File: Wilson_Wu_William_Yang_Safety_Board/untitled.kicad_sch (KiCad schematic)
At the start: 32 parts, among them J18 XT60-M, J3 430450200, J5 430450200, J6 XT60-M, J7 XT60-M, Q1 IRLML6344TRPBF, Q2 IRLML6344TRPBF, U12 J115F11AH12VDCS61.5U, U13 ISOM8110DFGRQ1, U16 J115F11AH12VDCS61.5U, U5 J115F11AH12VDCS61.5U, U6 J115F11AH12VDCS61.5U

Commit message: layout
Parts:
- removed TP12: TestPoint, TestPoint:TestPoint_Pad_D1.0mm, symbol Connector:TestPoint
- added load_neg_tp1, mosfet_drain_tp1, mosfet_drain_tp2, source_pos_tp1, source_pos_tp2: V_DIVIDED, TestPoint:TestPoint_Pad_D1.0mm, symbol Connector:TestPoint
- renumbered TP8 to ESTOP_TP1, TP_48V6 to HFC_NEG_TP1, TP_48V5 to HFC_RELAY_TP1, TP4 to RELAY_O_TP1, TP13 to load_pos_tp1
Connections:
- net DRAIN: now also mosfet_drain_tp1.1
- net load negative: now also load_neg_tp1.1
- net source negative: now also source_pos_tp1.1
- net source_conn: now also source_pos_tp2.1
- net at D2.2 (A), Q2.3, U5.2 (COIL_2): now also mosfet_drain_tp2.1

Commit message: update
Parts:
- added R_6: 0, Resistor_SMD:R_0805_2012Metric, symbol Device:R_US
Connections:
- net DRAIN: no longer names the net of D1.2 (A), Q1.3, U6.1 (COIL_1), mosfet_drain_tp1.1
- net DRAIN: now also R_6.2; no longer D7.2 (A), U12.2 (COIL_2)
- new net drain: D7.2 (A), R_6.1, U12.2 (COIL_2)
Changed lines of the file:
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@@
+	)
+	(junction
+		(at 142.24 50.8)
+		(diameter 0)
+		(color 0 0 0 0)
 	)
 	(junction
@@
 		(pts
 			(xy 142.24 31.75) (xy 142.24 46.99)
+		)
+		(stroke
+			(width 0)
+			(type default)
+		)
+	)
+	(wire
+		(pts
+			(xy 142.24 50.8) (xy 151.13 50.8)
 		)
 		(stroke
@@
 		)
 	)
-	(label "DRAIN"
-		(at 142.24 50.8 0)
-		(effects
-			(font
-				(size 1.27 1.27)
-			)
-			(justify left bottom)
-		)
-	)
-	(label "DRAIN"
-		(at 160.02 111.76 90)
-		(effects
-			(font
-				(size 1.27 1.27)
-			)
-			(justify left bottom)
-		)
-	)
 	(label "source negative"
 		(at 40.64 36.83 270)
@@
 			)
 			(justify left bottom)
+		)
+	)
+	(global_label "drain"
+		(shape input)
+		(at 158.75 50.8 0)
+		(fields_autoplaced yes)
+		(effects
+			(font
+				(size 1.27 1.27)
+			)
+			(justify left)
+		)
+		(property "Intersheetrefs" "${INTERSHEET_REFS}"
+			(at 166.5732 50.8 0)
+			(effects
+				(font
+					(size 1.27 1.27)
+				)
+				(justify left)
+				(hide yes)
+			)
 		)
 	)
@@
 				)
 				(justify right)
+				(hide yes)
+			)
+		)
+	)
+	(global_label "drain"
+		(shape input)
+		(at 160.02 111.76 90)
+		(fields_autoplaced yes)
+		(effects
+			(font
+				(size 1.27 1.27)
+			)
+			(justify left)
+		)
+		(property "Intersheetrefs" "${INTERSHEET_REFS}"
+			(at 160.02 103.9368 90)
+			(effects
+				(font
+					(size 1.27 1.27)
+				)
+				(justify left)
 				(hide yes)
 			)
@@
 					(unit 1)
 				)
+			)
+		)
+	)
+	(symbol
+		(lib_id "Device:R_US")
+		(at 154.94 50.8 270)
+		(unit 1)
+		(exclude_from_sim no)
+		(in_bom yes)
+		(on_board yes)
+		(dnp no)
+		(property "Reference" "R_6"
+			(at 154.94 54.864 90)
+			(effects
+				(font
+					(size 1.27 1.27)
+				)
+			)
+		)
+		(property "Value" "0"
+			(at 154.94 52.832 90)
+			(effects
+				(font
+					(size 1.27 1.27)
+				)
+			)
+		)
+		(property "Footprint" "Resistor_SMD:R_0805_2012Metric"
+			(at 154.686 51.816 90)
+			(effects
+				(font
+					(size 1.27 1.27)
+				)
+				(hide yes)
+			)
+		)
+		(property "Datasheet" "~"
+			(at 154.94 50.8 0)
+			(effects
+				(font
+					(size 1.27 1.27)
+				)
+				(hide yes)
+			)
+		)
+		(property "Description" "Resistor, US symbol"
+			(at 154.94 50.8 0)
+			(effects
+				(font
+					(size 1.27 1.27)
+				)
+				(hide yes)
+			)
+		)
+		(pin "1"
+		)
+		(pin "2"
+		)
+		(instances
+			(project "Wilson_Wu_William_Yang_Safety_Board"
+				(path "/fa857c32-0741-4b91-b122-1a57686bb514/3aab1625-1497-4612-8772-a9d051eba0fa"
+					(reference "R_6")
+					(unit 1)
+				)

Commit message: update
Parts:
- added D9: LED, LED_SMD:LED_Foshan-NTD3528_3.5x2.8mm, symbol Device:LED
- added R21: 10k, Resistor_SMD:R_0805_2012Metric, symbol Device:R_US
- R7: value 10k -> 0
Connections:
- net source negative is gone; now on net GND: J6.N (NEG), U5.4 (COM), source_pos_tp1.1
- net +12V: no longer R2.2
- net GND: now also D9.1 (K)
- net drain: now also R2.2
- net at D2.2 (A), Q2.3, U5.2 (COIL_2)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: now also R21.2
- new net: D9.2 (A), R21.1
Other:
- moved on the sheet: D6, R2, source_pos_tp1

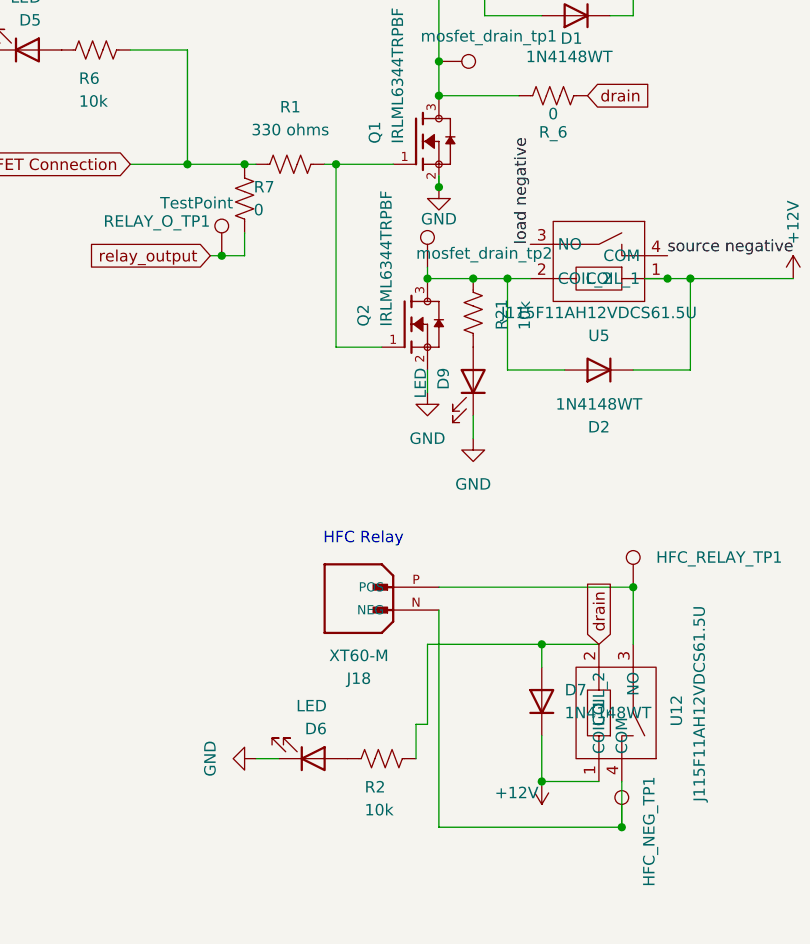
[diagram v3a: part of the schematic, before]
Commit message: LED Changes
-Fixed LED so that Relay U5 wouldn't always be on
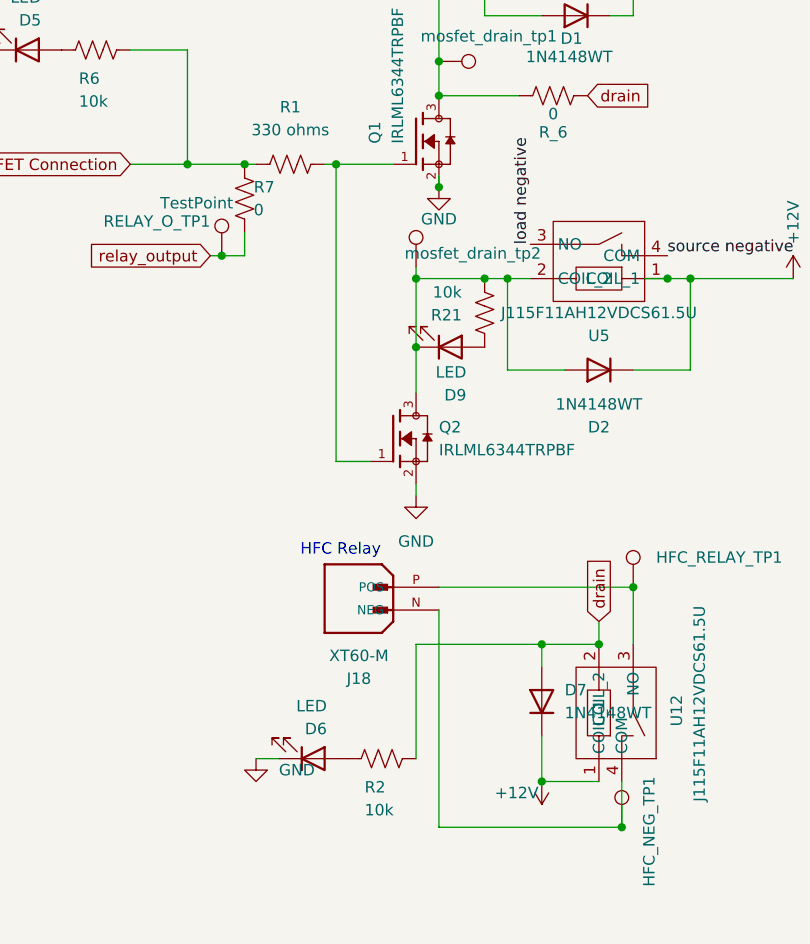
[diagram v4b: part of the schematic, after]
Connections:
- net GND: no longer D9.1 (K)
- net at D2.2 (A), Q2.3, U5.2 (COIL_2)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: now also D9.1 (K), R21.1; no longer R21.2
- net at D9.2 (A): now also R21.2; no longer R21.1
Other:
- moved on the sheet: D9, Q2, R21, mosfet_drain_tp2

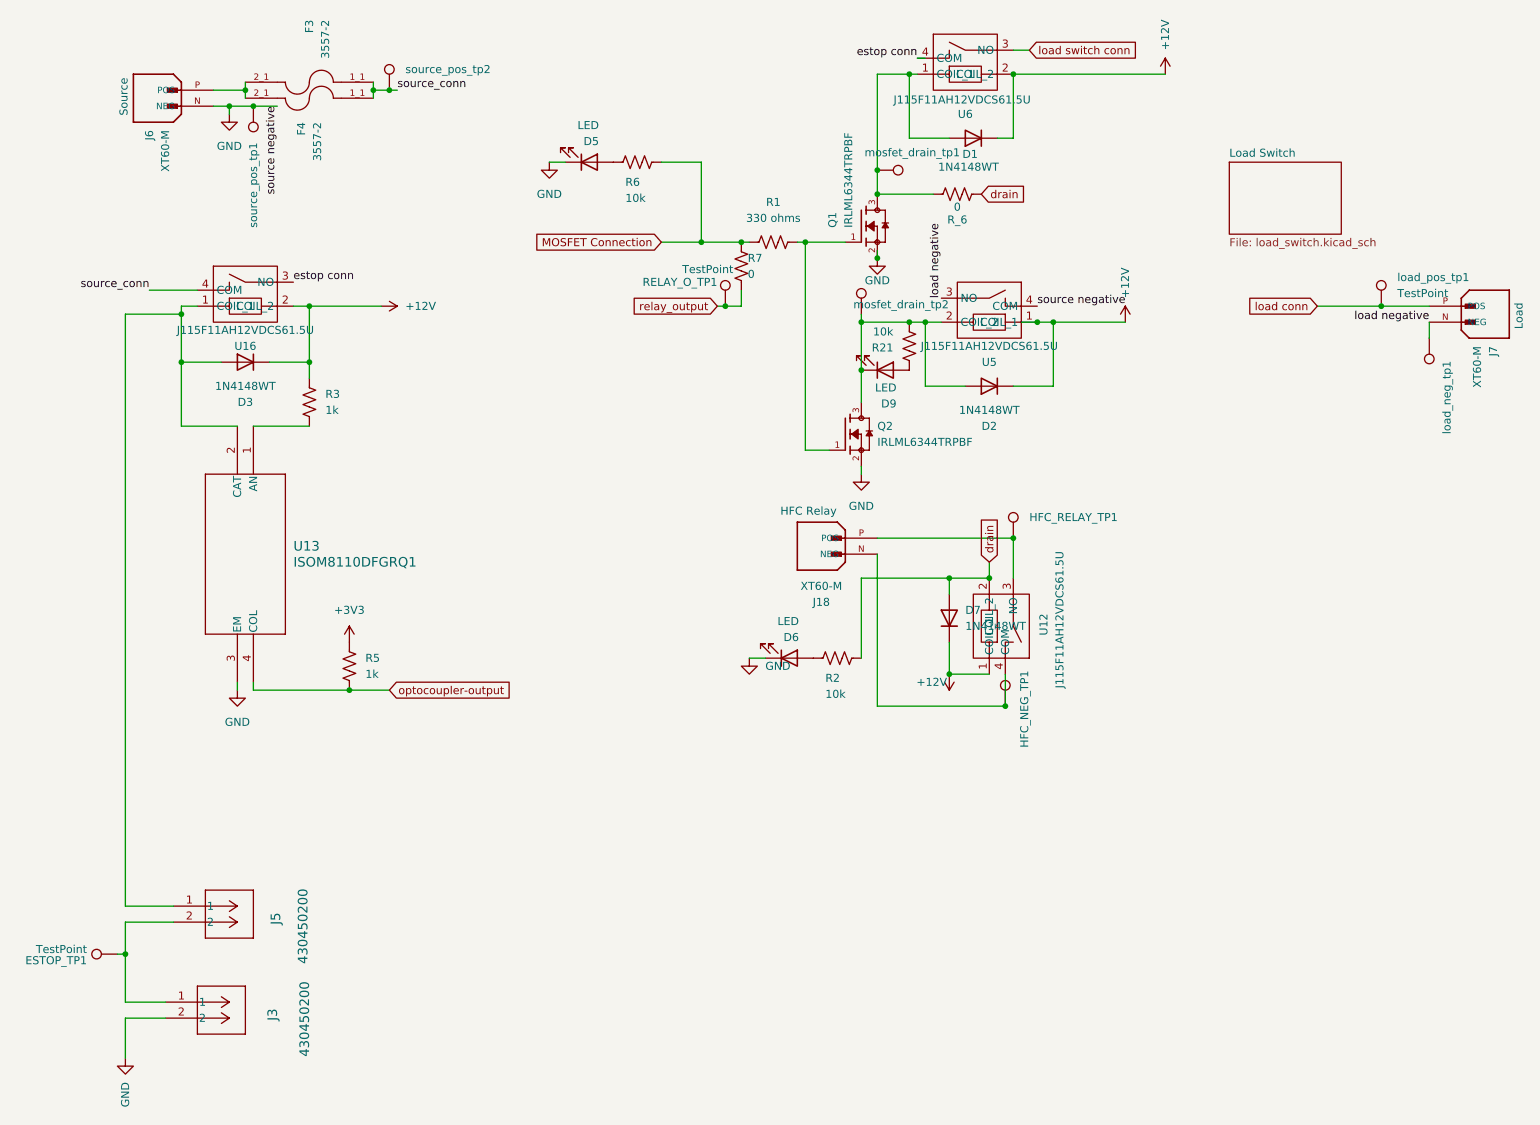
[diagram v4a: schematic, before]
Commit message: updated led positioning
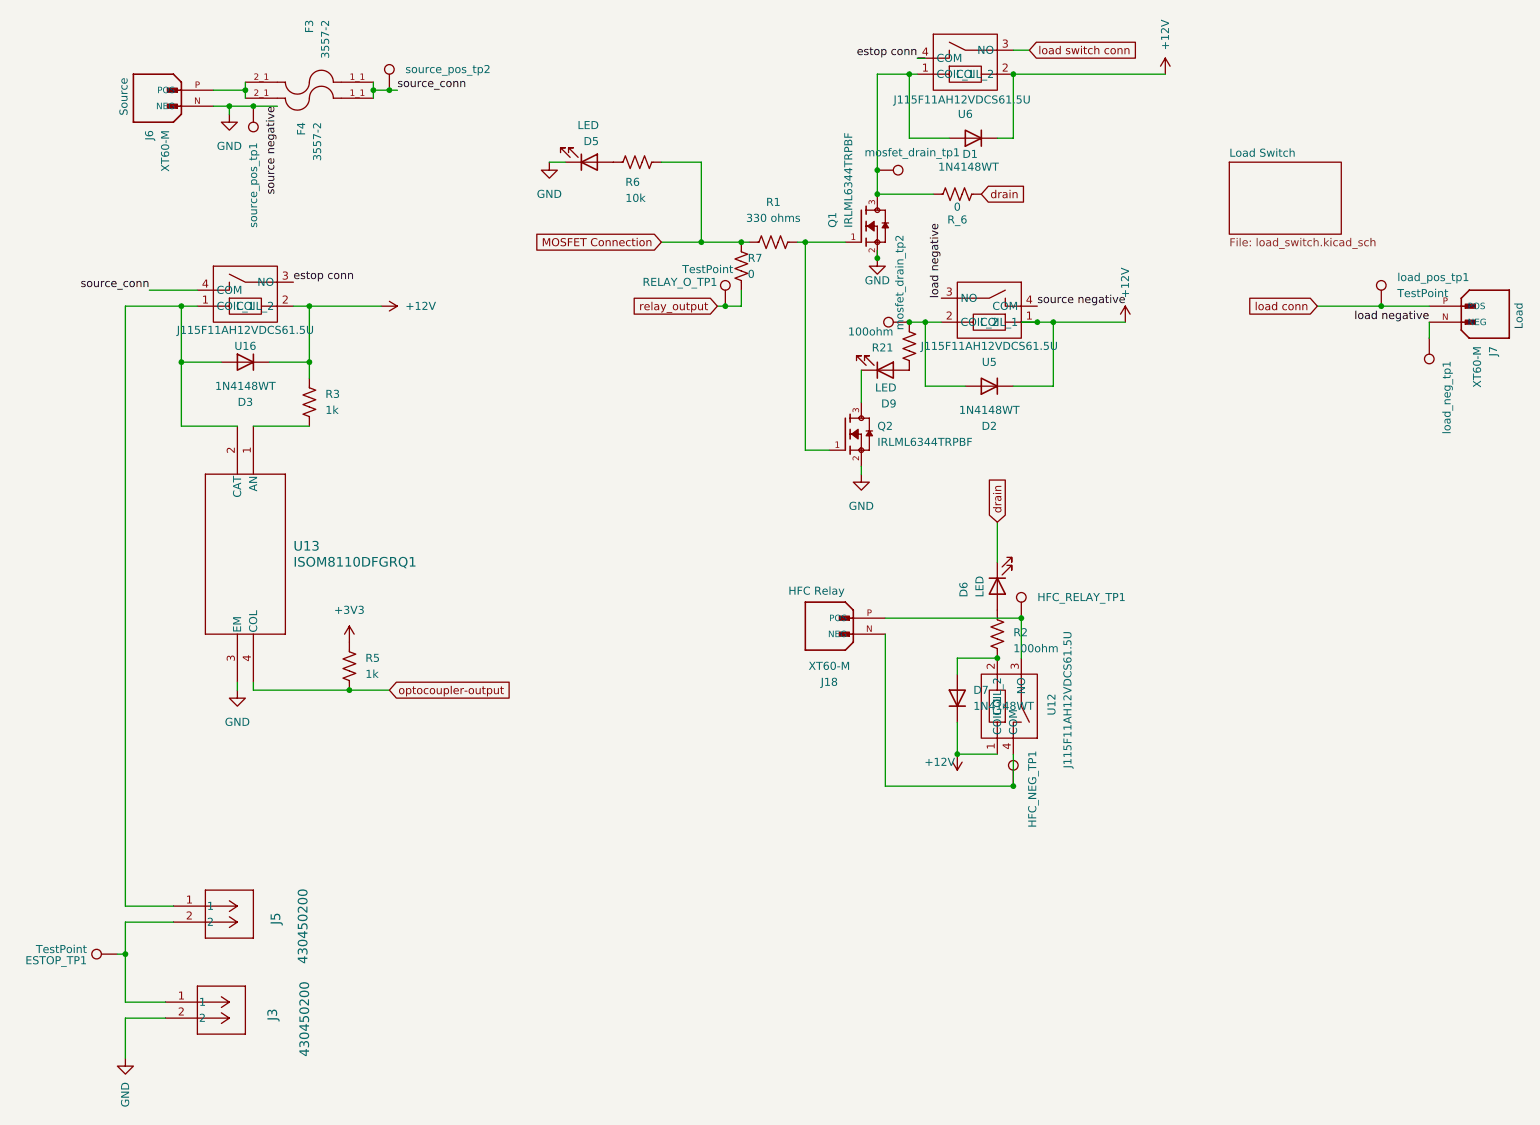
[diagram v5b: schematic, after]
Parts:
- R2, R21: value 10k -> 100ohm
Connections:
- net GND: no longer D6.1 (K)
- net drain: now also D6.1 (K); no longer D7.2 (A), R2.2, U12.2 (COIL_2)
- net at R2.1: now also D7.2 (A), U12.2 (COIL_2); no longer D6.2 (A)
- net at D2.2 (A), R21.1, U5.2 (COIL_2)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: no longer D9.1 (K), Q2.3
- new net: D6.2 (A), R2.2
- new net: D9.1 (K), Q2.3
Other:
- moved on the sheet: D7, HFC_NEG_TP1, HFC_RELAY_TP1, J18, U12, mosfet_drain_tp2

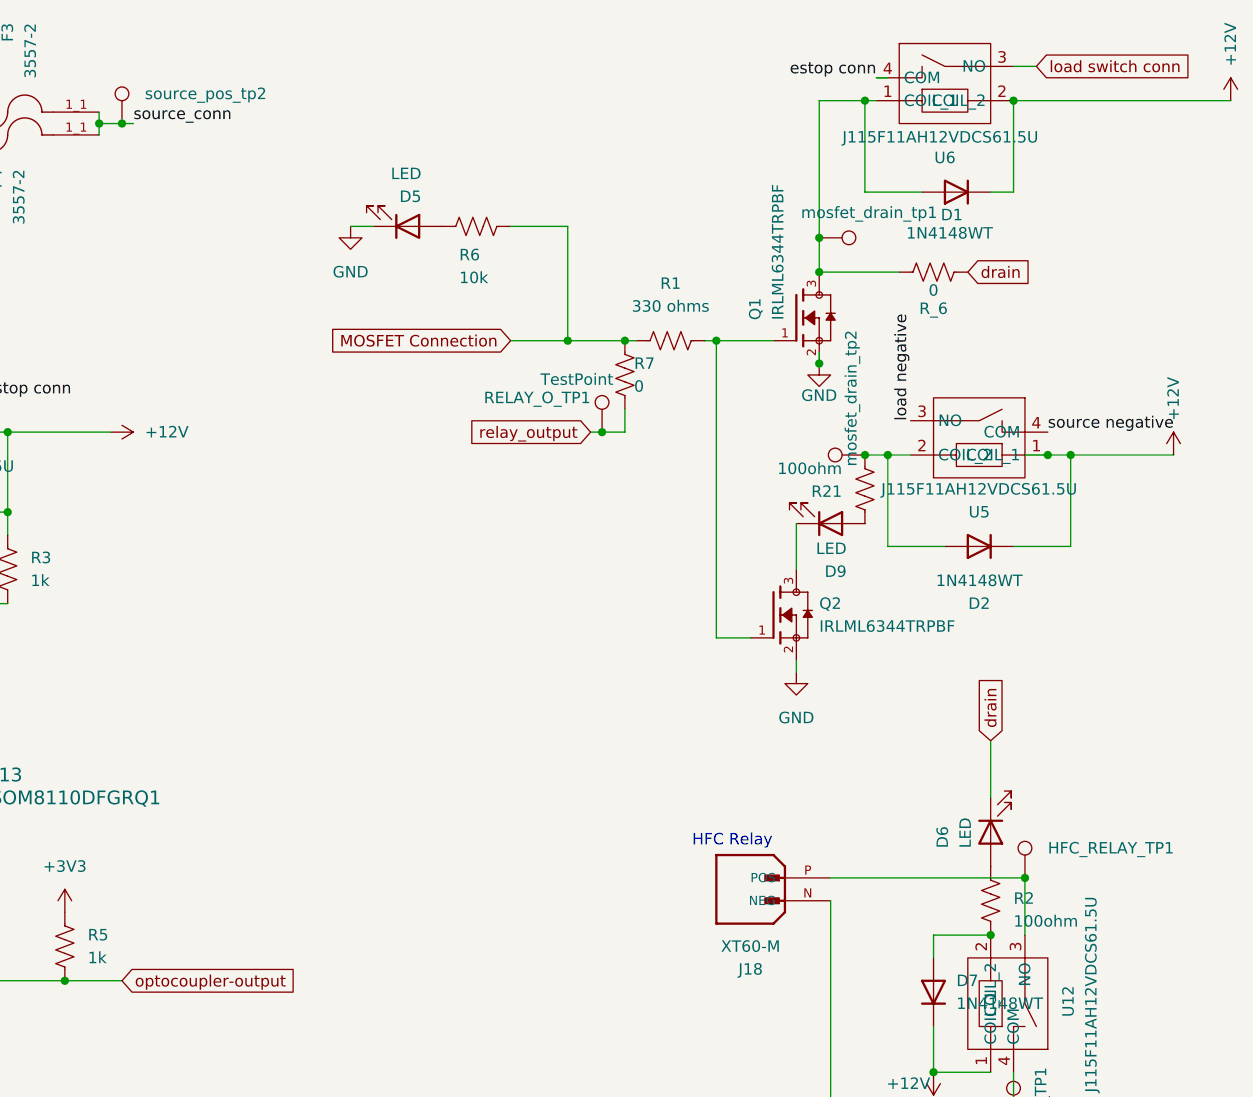
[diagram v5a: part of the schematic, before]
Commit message: connected leds to gate
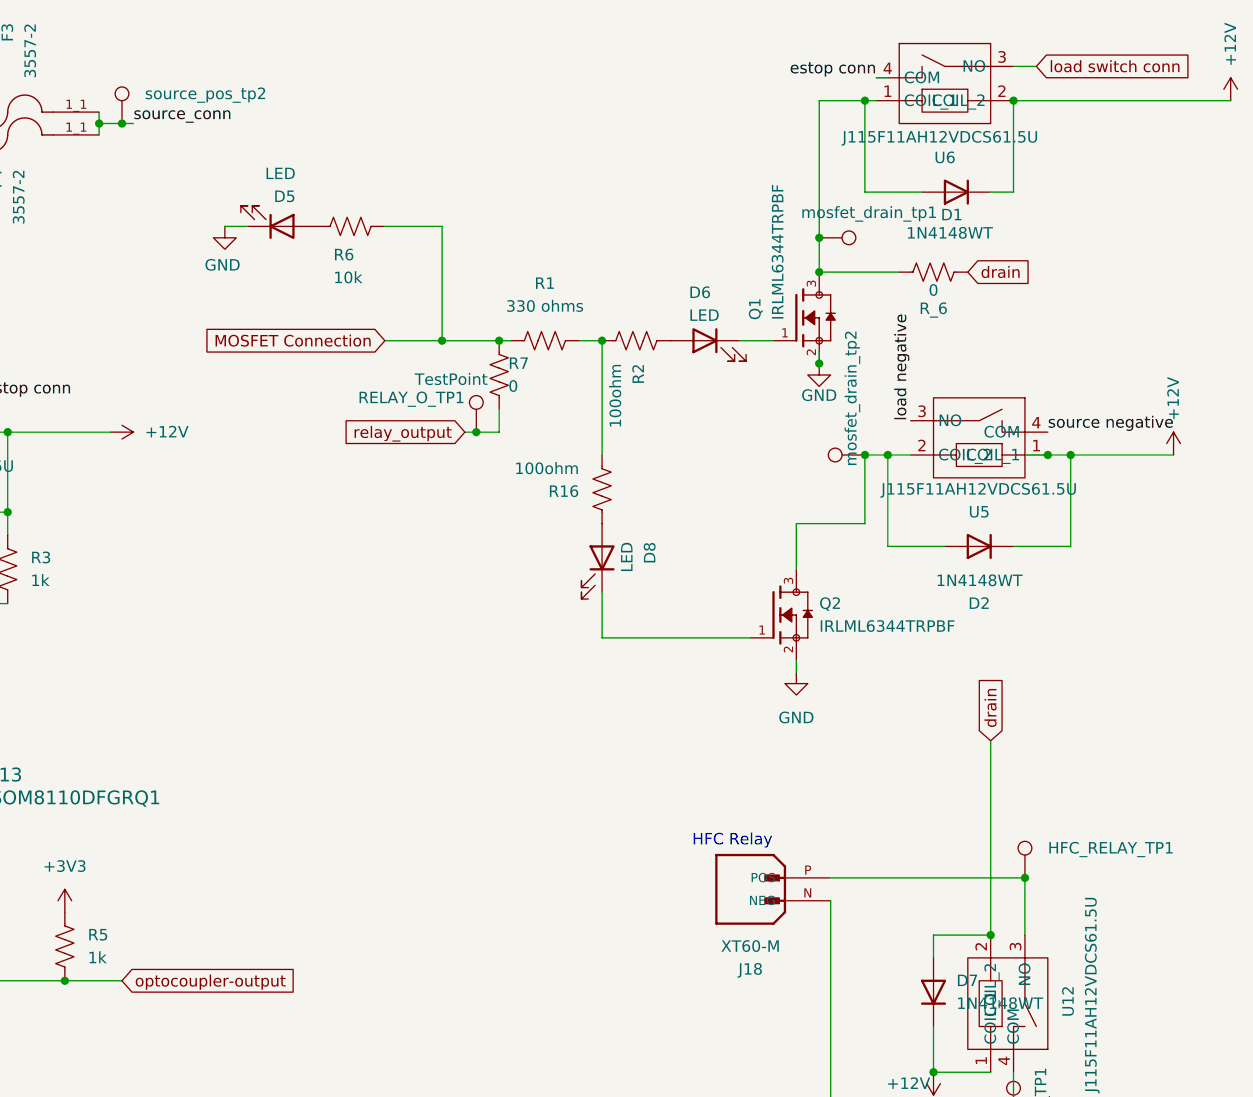
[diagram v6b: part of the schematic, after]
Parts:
- removed D9: LED, LED_SMD:LED_Foshan-NTD3528_3.5x2.8mm, symbol Device:LED
- removed R21: 100ohm, Resistor_SMD:R_0805_2012Metric, symbol Device:R_US
- added D8: LED, LED_SMD:LED_Foshan-NTD3528_3.5x2.8mm, symbol Device:LED
- added R16: 100ohm, Resistor_SMD:R_0805_2012Metric, symbol Device:R_US
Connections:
- net drain: now also D7.2 (A), U12.2 (COIL_2); no longer D6.1 (K)
- net at Q2.3: now also D2.2 (A), U5.2 (COIL_2), mosfet_drain_tp2.1
- new net: D6.1 (K), Q1.1
- new net: R1.1, R16.1, R2.1
- new net: D8.2 (A), R16.2
- new net: D8.1 (K), Q2.1
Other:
- moved on the sheet: D5, R1, R6, R7, RELAY_O_TP1

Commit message: led changes
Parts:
- removed D5, D6, D8: LED, LED_SMD:LED_Foshan-NTD3528_3.5x2.8mm, symbol Device:LED
- removed R16: 100ohm, Resistor_SMD:R_0805_2012Metric, symbol Device:R_US
- added D5, D6: WL-SMCW_0603, SMV_Passives:WL-SMCW_0603(diode), symbol SMV_Custom:WL-SMCW_0603
- R2: value 100ohm -> 100k
- R6: value 10k -> 100k
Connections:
- net GND: now also R2.2, R6.2
- net MOSFET Connection: no longer R6.2
- net at Q1.1: now also R2.1, D5.1
- net at R1.1: now also D5.2, D6.2; no longer R2.1
- net at Q2.1: now also R6.1, D6.1
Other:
- moved on the sheet: R2
